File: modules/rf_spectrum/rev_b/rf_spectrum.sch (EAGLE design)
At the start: 43 parts, among them J3 MODULE_GENERIC_DEBUGSMT, J4 TC2030-JLINK-L, Q1 SI223DDS, U1 MWSUB3G, U2 SKY13317, U3 STM32L432KC, U4 TLV62130, X1 ABS05-32.768KHZ-T

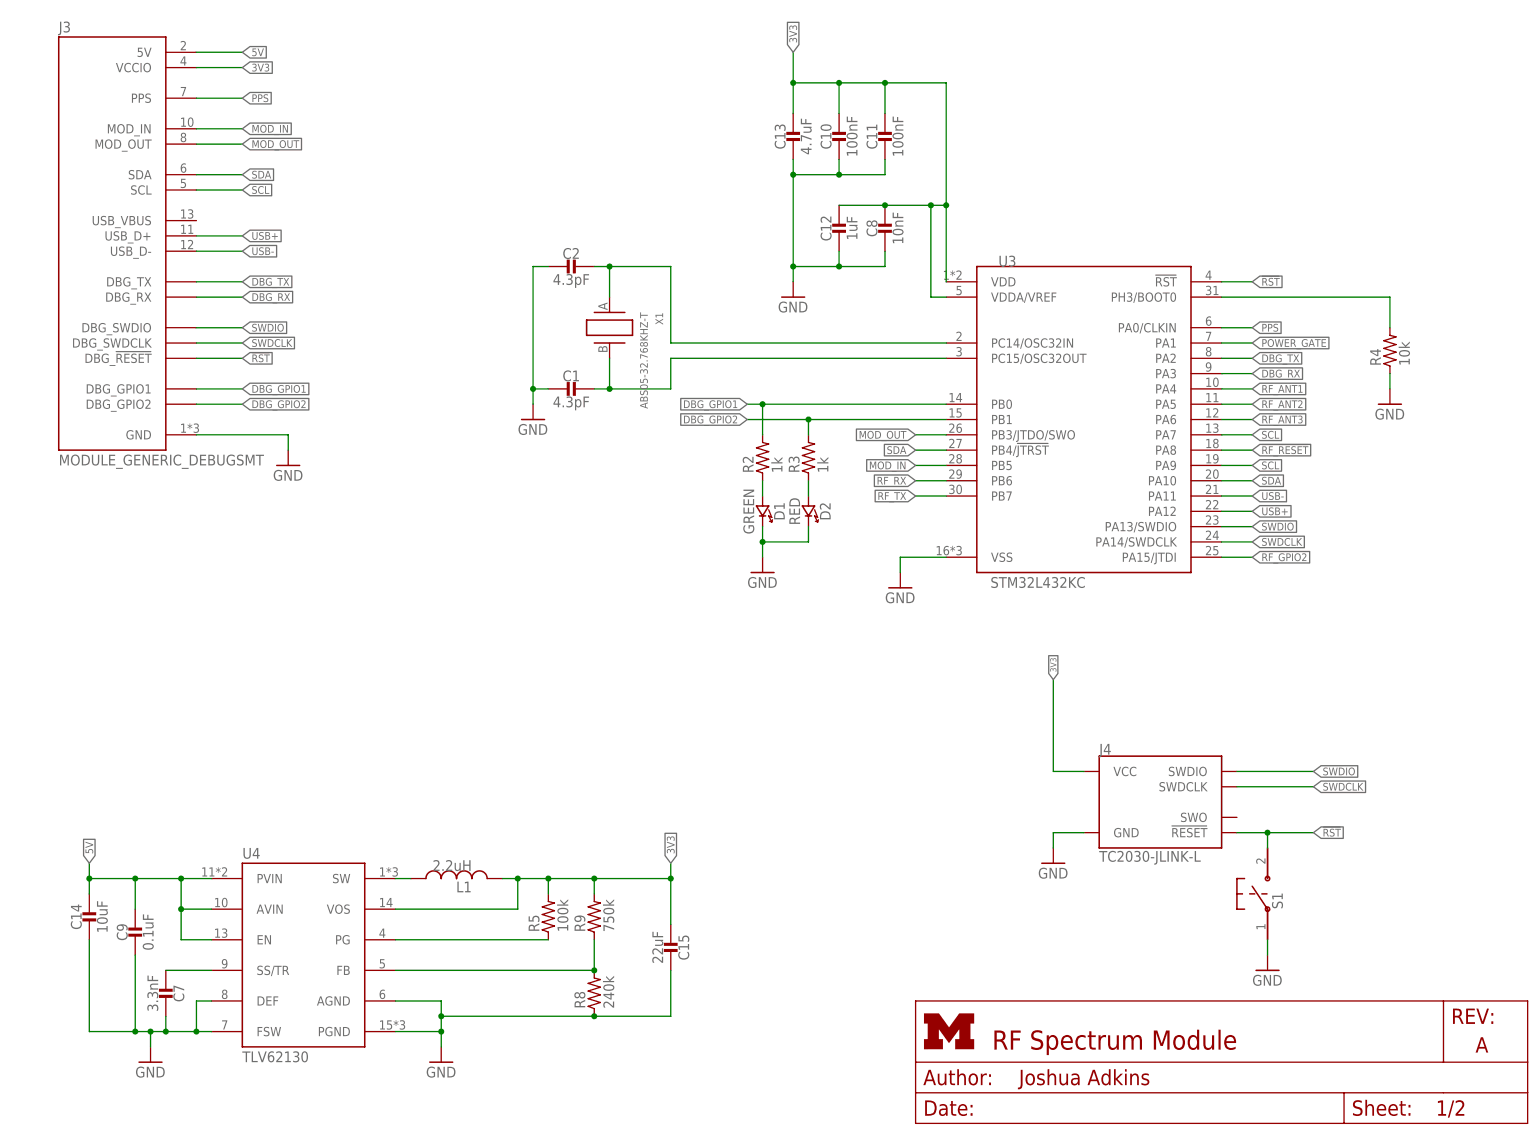
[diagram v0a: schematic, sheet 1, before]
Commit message: added rf spectrum cleanups, especially to BOM
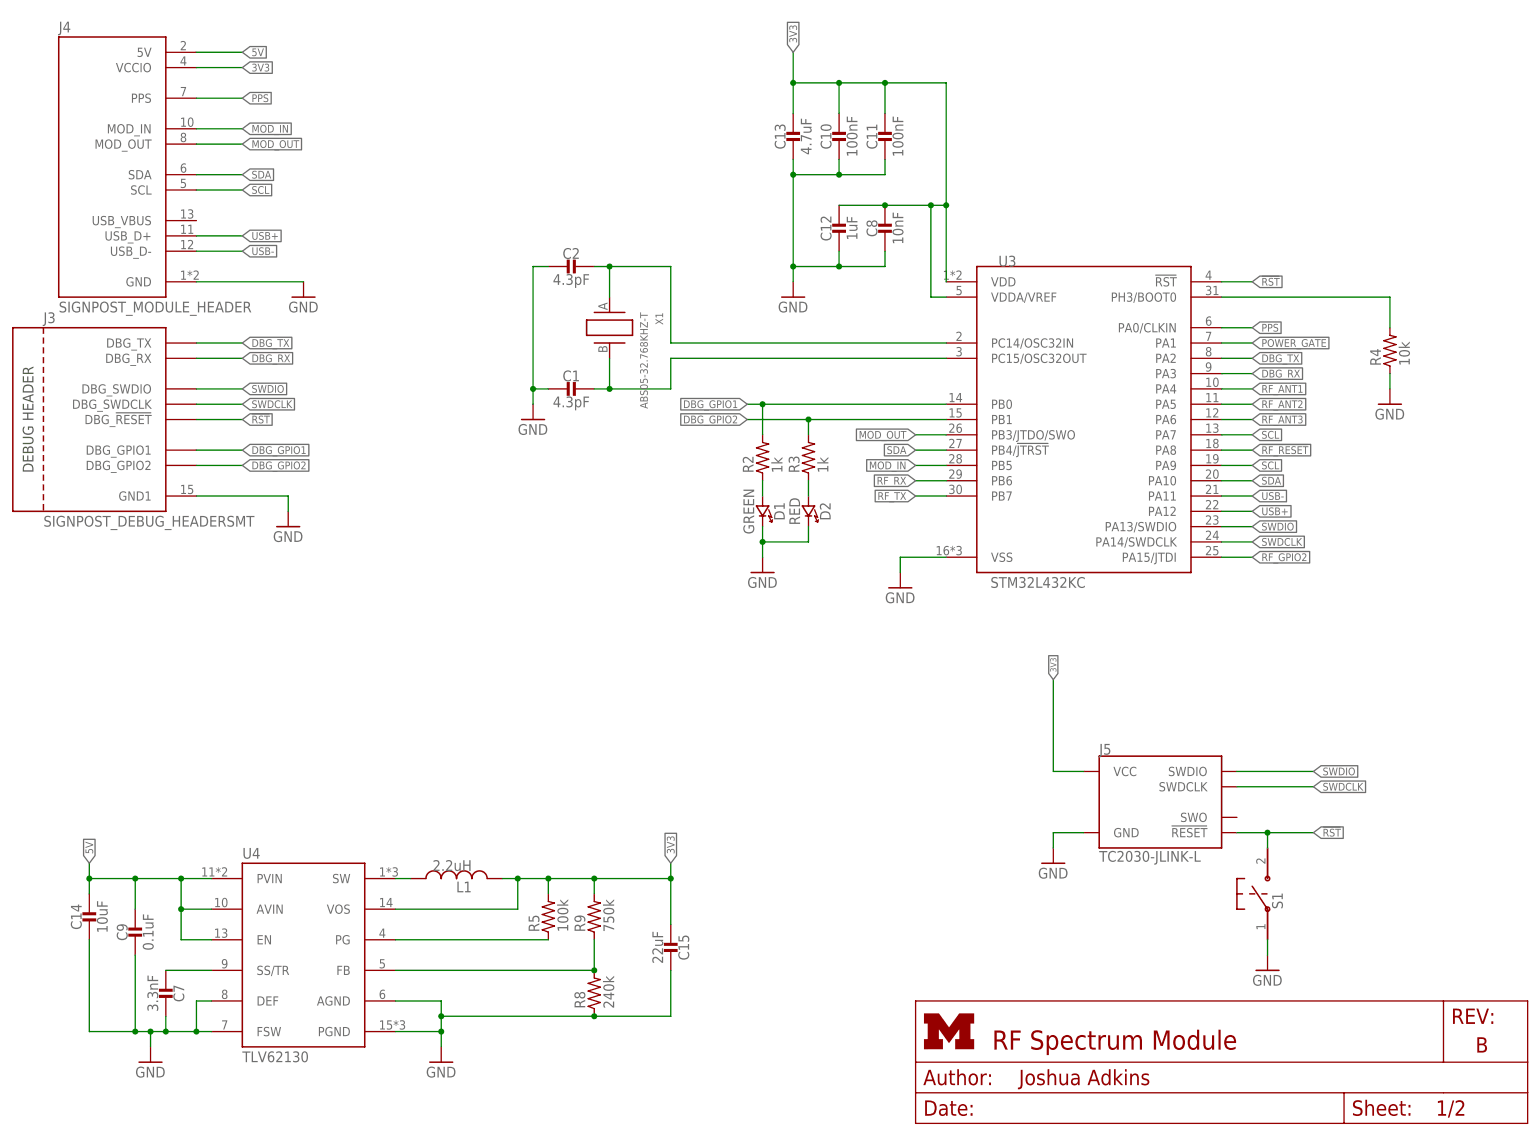
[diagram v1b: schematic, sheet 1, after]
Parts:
- added J5: TC2030-JLINK-L, connector:TC2030-JLINK-L
- C1, C2: MANUFACTURER (none) -> Murata; MF Murata -> (none); MFN GRM1555C1H4R3BA01D -> (none); MPN (none) -> GRM1555C1H4R3BA01D
- C10, C11: MANUFACTURER (none) -> Murata; MF Murata -> (none); MFN GRM155R71C104KA88J -> (none); MPN (none) -> GRM155R71C104KA88J
- C12: MANUFACTURER (none) -> Murata; MF Murata -> (none); MFN GRM155R60J105KE19D -> (none); MPN (none) -> GRM155R60J105KE19D
- C13: MANUFACTURER (none) -> Murata; MF Murata -> (none); MFN GRM155R60J475ME47D -> (none); MPN (none) -> GRM155R60J475ME47D
- C14: MANUFACTURER (none) -> Murata; MF Murata -> (none); MFN GRM188R60J106ME47J -> (none); MPN (none) -> GRM188R60J106ME47J
- C15: MANUFACTURER (none) -> Murata; MF Murata -> (none); MFN GRM188R60J226MEA0D -> (none); MPN (none) -> GRM188R60J226MEA0D
- C3, C4, C5: MANUFACTURER (none) -> Murata; MF Murata -> (none); MFN GRM1555C1H470FA01D -> (none); MPN (none) -> GRM1555C1H470FA01D
- C6: MANUFACTURER (none) -> Murata; MF Murata -> (none); MFN GRM1555C1H221JA01D -> (none); MPN (none) -> GRM1555C1H221JA01D
- C7: MANUFACTURER (none) -> Murata; MF Murata -> (none); MFN GRM188R71H332KA01D -> (none); MPN (none) -> GRM188R71H332KA01D
- C8: MANUFACTURER (none) -> Murata; MF Murata -> (none); MFN GRM155R71H103KA88D -> (none); MPN (none) -> GRM155R71H103KA88D
- C9: MANUFACTURER (none) -> Murata; MF Murata -> (none); MFN GRM188R71C104KA01D -> (none); MPN (none) -> GRM188R71C104KA01D
- D1: MANUFACTURER (none) -> Lite-ON; MF Lite-ON -> (none); MFN LTST-C191KGKT -> (none); MPN (none) -> LTST-C191KGKT
- D2: MANUFACTURER (none) -> Lite-On; MF Lite-On -> (none); MFN LTST-C191KRKT -> (none); MPN (none) -> LTST-C191KRKT
- J1, J2: MANUFACTURER (none) -> Molex; MF Molex -> (none); MFN 0901200764 -> (none); MPN (none) -> 0901200764
- J3: value MODULE_GENERIC_DEBUGSMT -> SIGNPOST_DEBUG_HEADERSMT; device signpost:MODULE_GENERIC_DEBUGSMT -> signpost:SIGNPOST_DEBUG_HEADERSMT
- J4: value TC2030-JLINK-L -> SIGNPOST_MODULE_HEADER; device connector:TC2030-JLINK-L -> signpost:SIGNPOST_MODULE_HEADER
- R1: value 0 -> DNP - 0; MANUFACTURER (none) -> Yageo; MF Yageo -> (none); MFN RC0402JR-070RL -> (none); MPN (none) -> RC0402JR-070RL
- R10, R6, R7: MANUFACTURER (none) -> Yageo; MF Yageo -> (none); MFN RC0402FR-07100KL -> (none); MPN (none) -> RC0402FR-07100KL
- R2, R3, R4: MANUFACTURER (none) -> Yageo; MF Yageo -> (none); MFN RC0402JR-071KL -> (none); MPN (none) -> RC0402JR-071KL
- R5: MANUFACTURER (none) -> Yageo; MF Yageo -> (none); MFN RC0603JR-07100KL -> (none); MPN (none) -> RC0603JR-07100KL
- R8: MANUFACTURER (none) -> Yageo; MF Yageo -> (none); MFN RC0603JR-07240KL -> (none); MPN (none) -> RC0603JR-07240KL
- R9: MANUFACTURER (none) -> Yageo; MF Yageo -> (none); MFN 311-750KGRCT-ND -> (none); MPN (none) -> 311-750KGRCT-ND
- U3: MF STM -> (none)
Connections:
- net !RF_RESET: now also J2.4; no longer J1.4
- net !RST: now also J5.!RESET; no longer J4.!RESET
- net 3V3: now also J4.VCCIO, J5.VCC; no longer J3.VCCIO, J4.VCC
- net 5V: now also J4.5V; no longer J3.5V
- net GND: now also J3.GND1, J5.GND; no longer J3.GND
- net MOD_IN: now also J4.MOD_IN; no longer J3.MOD_IN
- net MOD_OUT: now also J4.MOD_OUT; no longer J3.MOD_OUT
- net PPS: now also J4.PPS; no longer J3.PPS
- net RF_ANT1: now also J1.4; no longer J2.4
- net RF_ANT2: now also J1.3; no longer J2.3
- net RF_ANT3: now also J1.2; no longer J2.2
- net RF_GPIO2: now also J2.1; no longer J1.1
- net RF_GPIO3: now also J1.1; no longer J2.1
- net RF_RX: now also J2.2; no longer J1.2
- net RF_TX: now also J2.3; no longer J1.3
- net SCL: now also J4.SCL; no longer J3.SCL
- net SDA: now also J4.SDA; no longer J3.SDA
- net SWDCLK: now also J5.SWDCLK; no longer J4.SWDCLK
- net SWDIO: now also J5.SWDIO; no longer J4.SWDIO
- net USB+: now also J4.USB_D+; no longer J3.USB_D+
- net USB-: now also J4.USB_D-; no longer J3.USB_D-
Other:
- moved on the sheet: J1, J2

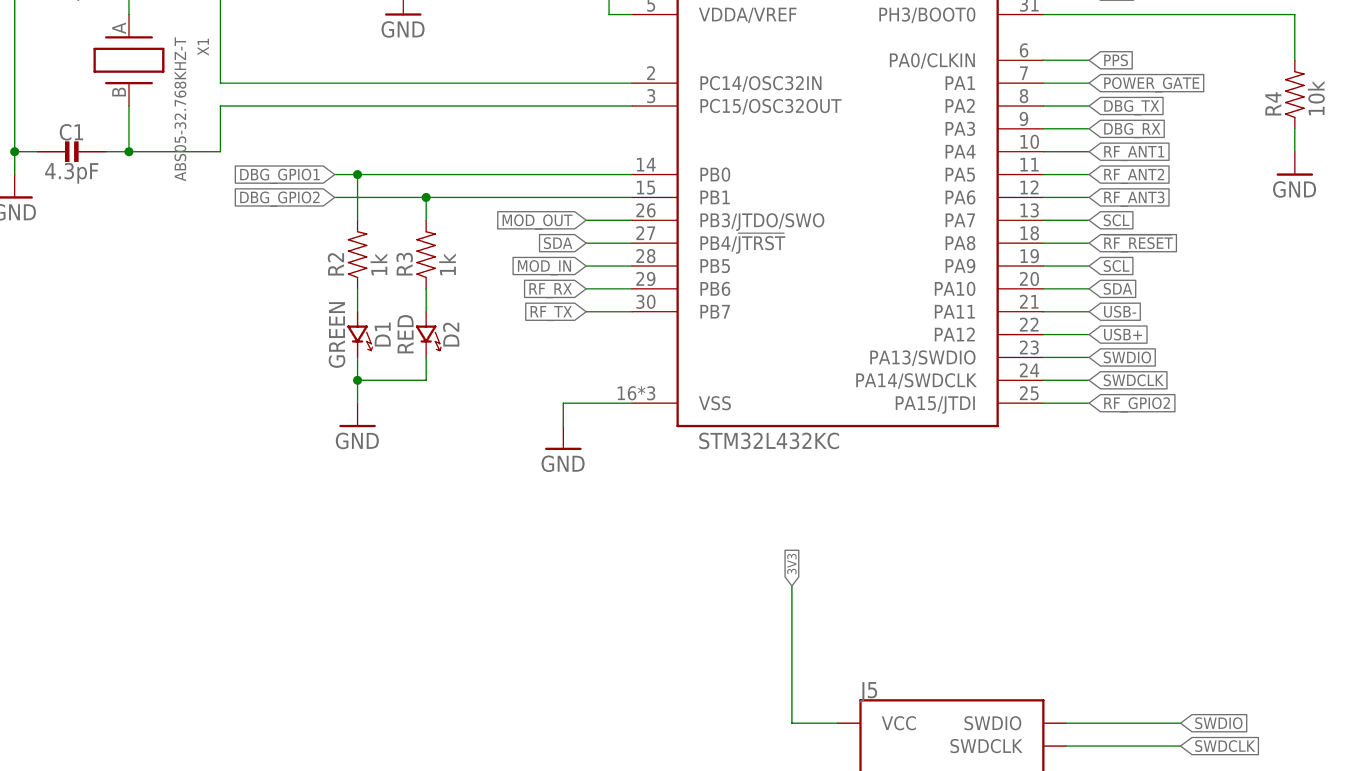
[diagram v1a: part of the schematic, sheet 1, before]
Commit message: fixed pin mapping, added RTS/CTS
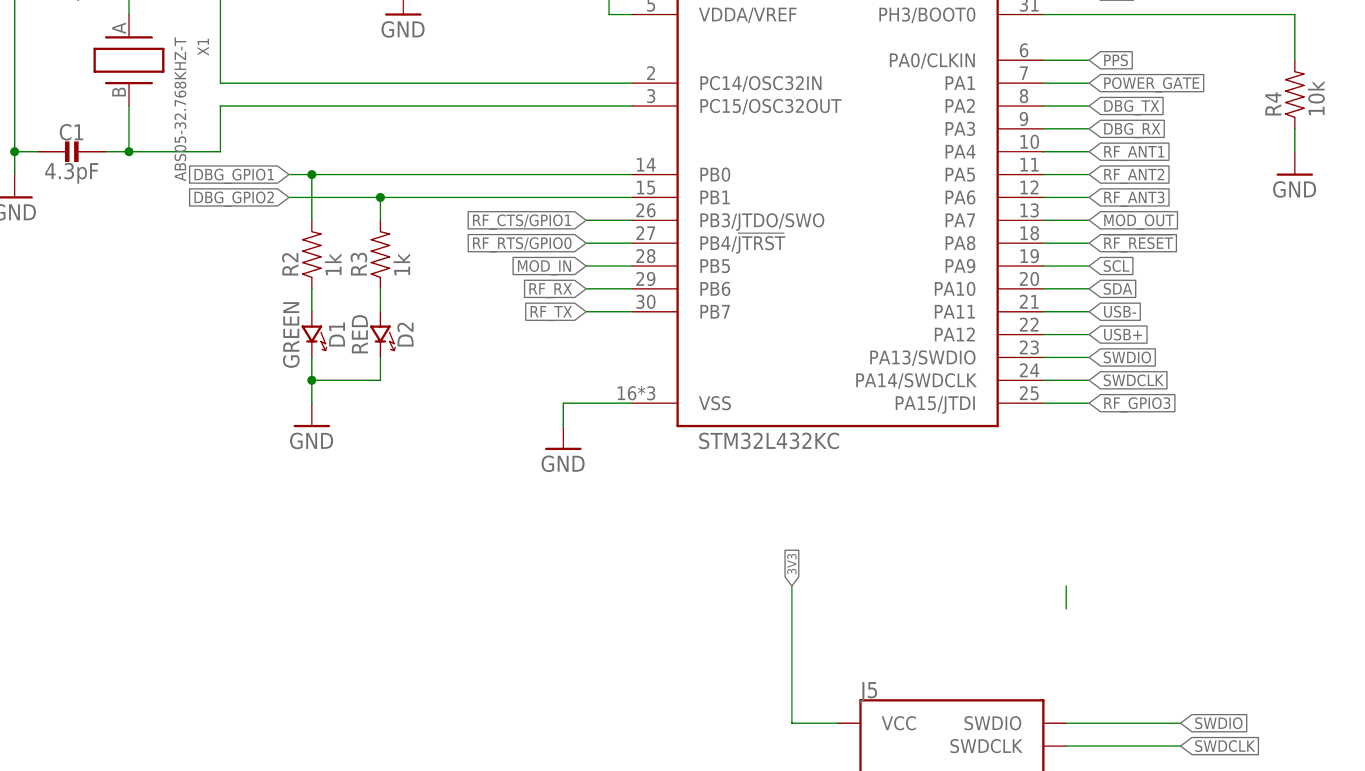
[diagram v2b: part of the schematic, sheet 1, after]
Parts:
- added R11: 100k, passives:RESISTOR0402_RES
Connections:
- new net RF_CTS/GPIO1: J2.2, U1.GPIO1, U3.PB3/JTDO/SWO
- new net RF_RTS/GPIO0: J2.1, U1.GPIO0, U3.PB4/!JTRST
- net !RF_RESET: now also J1.1; no longer J2.4
- net GATED: now also R11.1; no longer R7.2
- net GND: now also R7.2
- net MOD_OUT: now also U3.PA7; no longer U3.PB3/JTDO/SWO
- net RF_GPIO2: no longer J2.1, U3.PA15/JTDI
- net RF_GPIO3: now also R11.2, U1.GPIO3, U3.PA15/JTDI; no longer J1.1
- net RF_RX: now also J2.3; no longer J2.2
- net RF_TX: now also J2.4; no longer J2.3
- net SCL: no longer U3.PA7
- net SDA: no longer U3.PB4/!JTRST
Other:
- moved on the sheet: D1, D2, R2, R3, R7
